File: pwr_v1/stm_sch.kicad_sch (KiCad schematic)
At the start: 2 parts, among them CN11 Conn_02x36_Odd_Even, CN12 Conn_02x36_Odd_Even

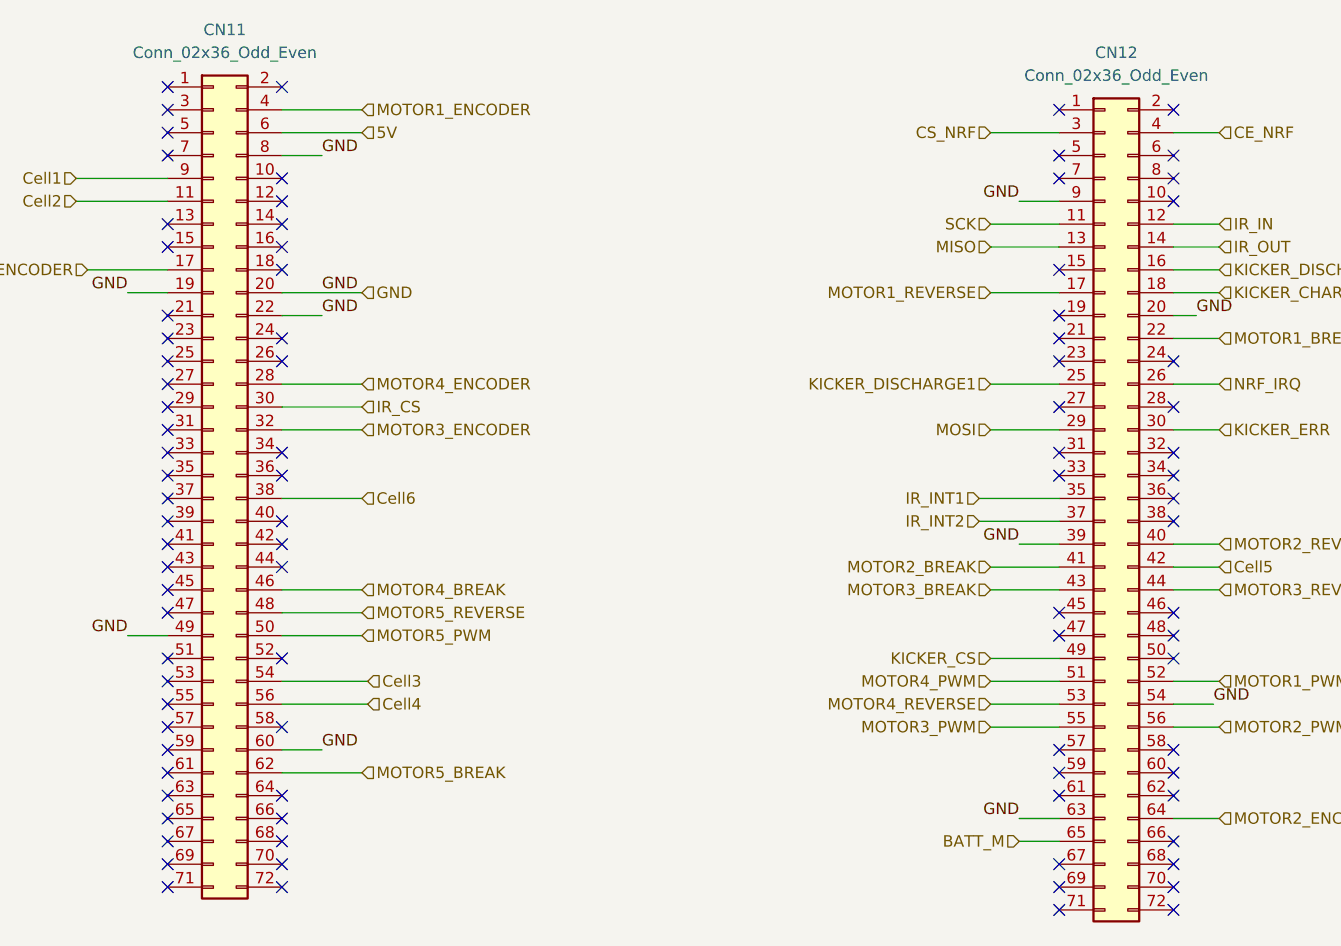
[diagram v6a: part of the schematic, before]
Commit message: Sch: DNP updated, JLC part numbers updated for all components; Lay: Fiducial placement, routing aligned.
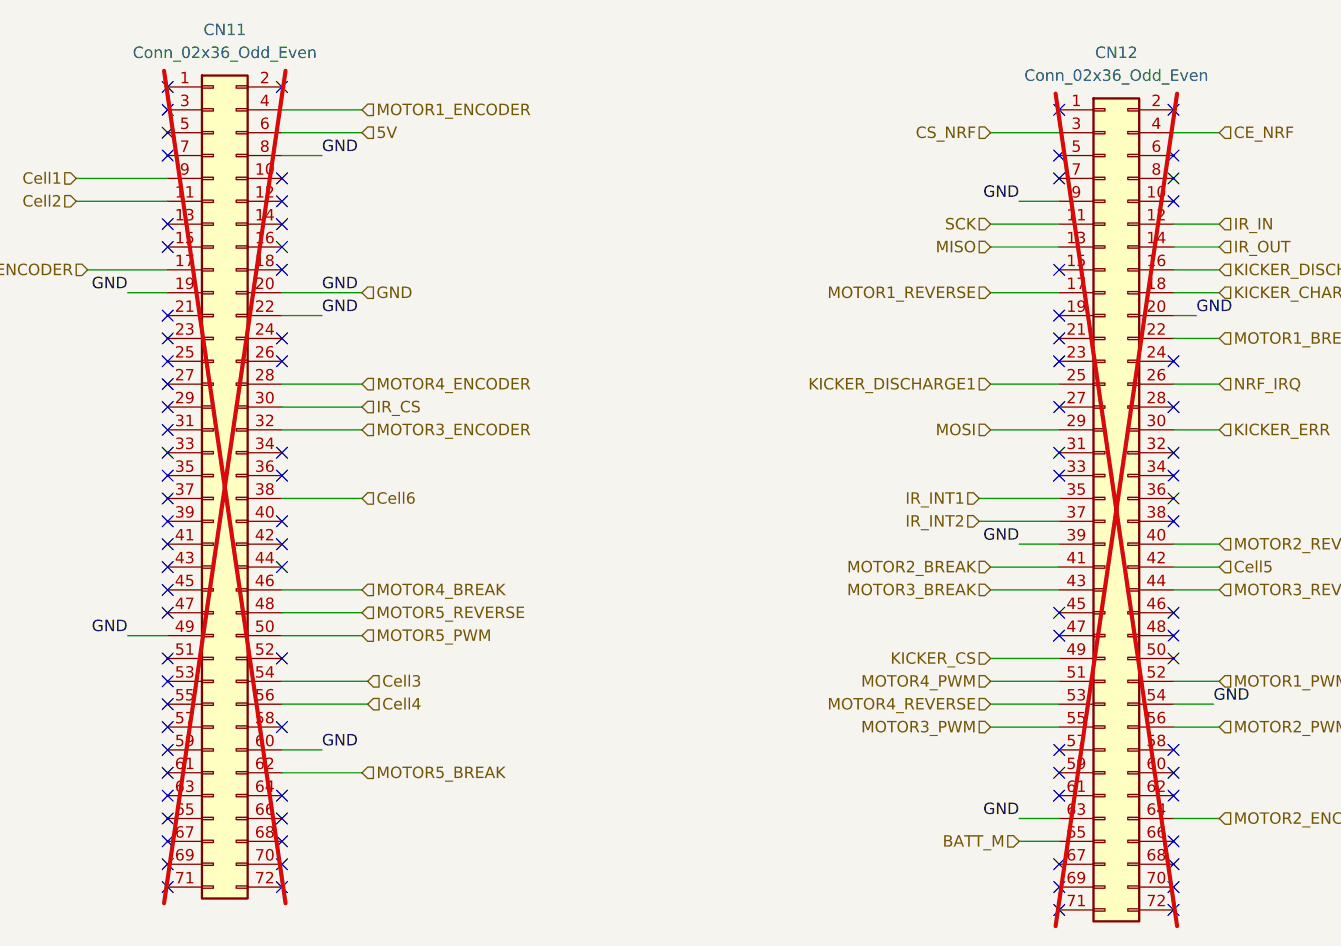
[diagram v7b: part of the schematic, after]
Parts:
- CN11, CN12: now not fitted; now left out of the parts list
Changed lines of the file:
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@@
 		(unit 1)
 		(exclude_from_sim no)
-		(in_bom yes)
+		(in_bom no)
 		(on_board yes)
-		(dnp no)
+		(dnp yes)
 		(fields_autoplaced yes)
 		(property "Reference" "CN11"
@@
 		(unit 1)
 		(exclude_from_sim no)
-		(in_bom yes)
+		(in_bom no)
 		(on_board yes)
-		(dnp no)
+		(dnp yes)
 		(fields_autoplaced yes)
 		(property "Reference" "CN12"

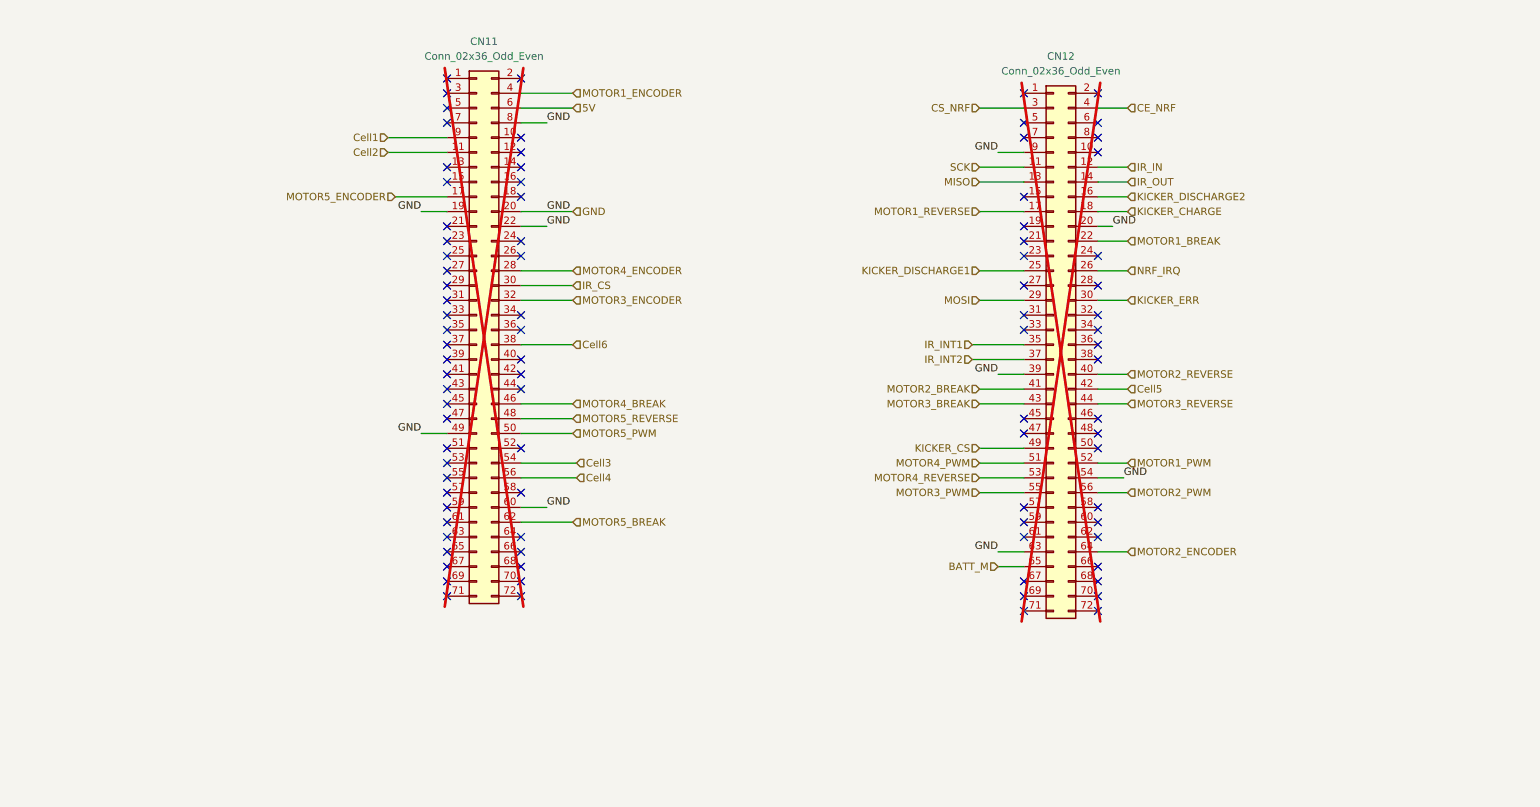
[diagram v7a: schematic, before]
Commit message: File structure enhanced.
Added uniform titleblocks and 3D renders for easier view, file cleanups.
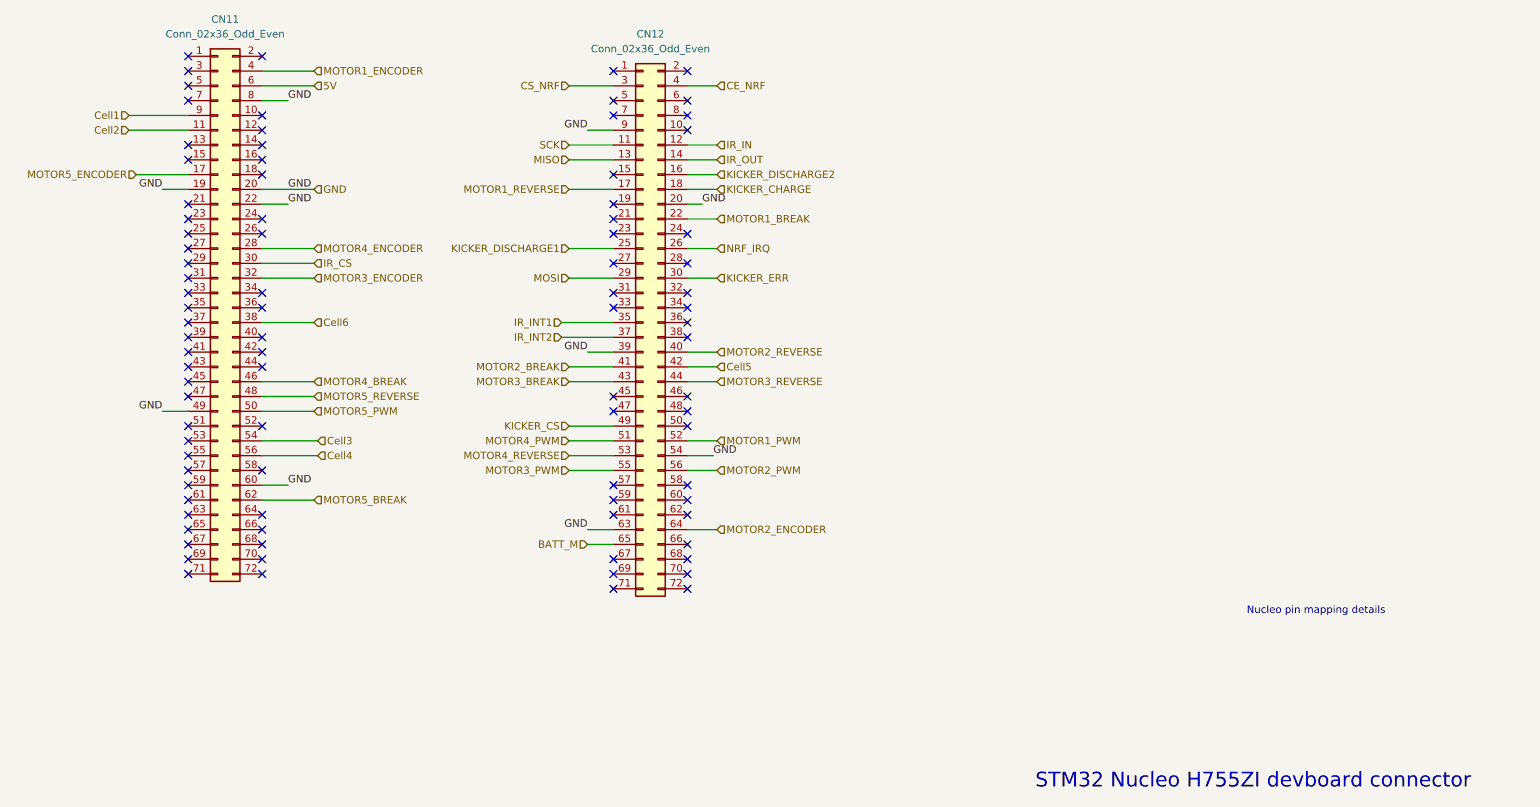
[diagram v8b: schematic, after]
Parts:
- CN11, CN12: now fitted
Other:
- note added: "Nucleo pin mapping details"
- note added: "STM32 Nucleo H755ZI devboard connector"
- title: (none) -> Power board
